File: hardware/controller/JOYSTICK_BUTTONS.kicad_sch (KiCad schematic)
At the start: 18 parts, among them SW401 UP, SW402 LEFT, SW403 DOWN, SW404 RIGHT

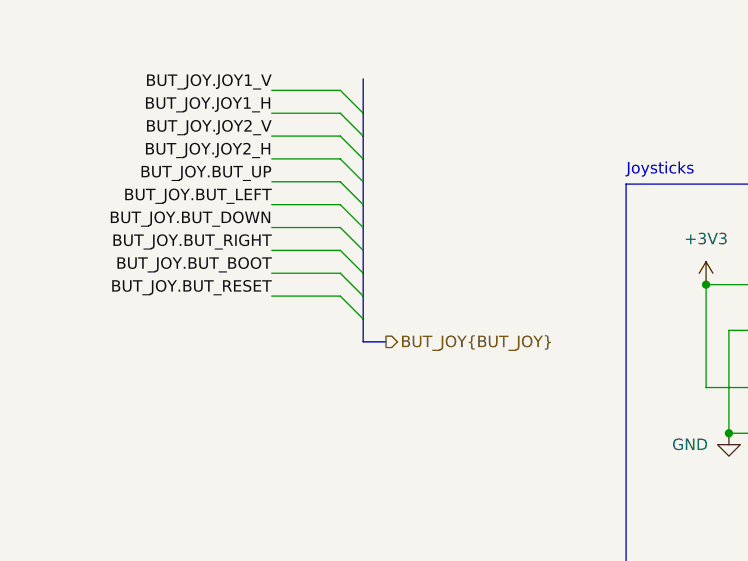
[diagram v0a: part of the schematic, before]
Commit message: fixed 3d models. rounded edges of pcb
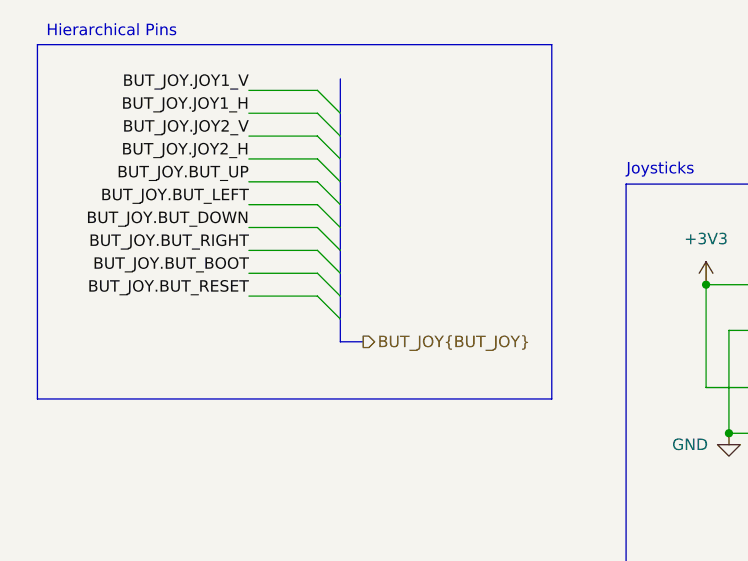
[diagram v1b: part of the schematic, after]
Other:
- note added: "Hierarchical Pins"
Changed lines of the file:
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@@
 	(paper "A4")
+	(rectangle
+		(start 14.605 15.24)
+		(end 71.755 54.61)
+		(stroke
+			(width 0)
+			(type default)
+		)
+		(fill
+			(type none)
+		)
+	)
 	(rectangle
 		(start 80.01 30.734)
@@
 		)
 	)
+	(text "Hierarchical Pins"
+		(exclude_from_sim no)
+		(at 22.86 13.843 0)
+		(effects
+			(font
+				(size 1.27 1.27)
+			)
+		)
+	)
 	(text "Joysticks"
 		(exclude_from_sim no)
@@
 	)
 	(bus_entry
-		(at 48.26 22.86)
+		(at 45.72 22.86)
 		(size 2.54 2.54)
 		(stroke
@@
 	)
 	(bus_entry
-		(at 48.26 35.56)
+		(at 45.72 35.56)
 		(size 2.54 2.54)
 		(stroke
@@
 	)
 	(bus_entry
-		(at 48.26 38.1)
+		(at 45.72 38.1)
 		(size 2.54 2.54)
 		(stroke
@@
 	)
 	(bus_entry
-		(at 48.26 40.64)
+		(at 45.72 40.64)
 		(size 2.54 2.54)
 		(stroke
@@
 	)
 	(bus_entry
-		(at 48.26 20.32)
+		(at 45.72 20.32)
 		(size 2.54 2.54)
 		(stroke
@@
 	)
 	(bus_entry
-		(at 48.26 33.02)
+		(at 45.72 33.02)
 		(size 2.54 2.54)
 		(stroke
@@
 	)
 	(bus_entry
-		(at 48.26 25.4)
+		(at 45.72 25.4)
 		(size 2.54 2.54)
 		(stroke
@@
 	)
 	(bus_entry
-		(at 48.26 27.94)
+		(at 45.72 27.94)
 		(size 2.54 2.54)
 		(stroke
@@
 	)
 	(bus_entry
-		(at 48.26 43.18)
+		(at 45.72 43.18)
 		(size 2.54 2.54)
 		(stroke
@@
 	)
 	(bus_entry
-		(at 48.26 30.48)
+		(at 45.72 30.48)
 		(size 2.54 2.54)
 		(stroke
@@
 	(bus
 		(pts
-			(xy 50.8 27.94) (xy 50.8 30.48)
+			(xy 48.26 27.94) (xy 48.26 30.48)
 		)
 		(stroke
@@
 	(bus
 		(pts
-			(xy 50.8 30.48) (xy 50.8 33.02)
+			(xy 48.26 30.48) (xy 48.26 33.02)
 		)
 		(stroke
@@
 	(bus
 		(pts
-			(xy 50.8 33.02) (xy 50.8 35.56)
+			(xy 48.26 33.02) (xy 48.26 35.56)
 		)
 		(stroke
@@
 	(bus
 		(pts
-			(xy 50.8 22.86) (xy 50.8 25.4)
+			(xy 48.26 22.86) (xy 48.26 25.4)
 		)
 		(stroke
@@
 	(bus
 		(pts
-			(xy 50.8 38.1) (xy 50.8 40.64)
-		)
-		(stroke
-			(width 0)
-			(type default)
-		)
-	)
-	(wire
-		(pts
-			(xy 40.64 27.94) (xy 48.26 27.94)
+			(xy 48.26 38.1) (xy 48.26 40.64)
+		)
+		(stroke
+			(width 0)
+			(type default)
+		)
+	)
+	(wire
+		(pts
+			(xy 38.1 27.94) (xy 45.72 27.94)
 		)
 		(stroke
@@
 	(bus
 		(pts
-			(xy 50.8 35.56) (xy 50.8 38.1)
+			(xy 48.26 35.56) (xy 48.26 38.1)
 		)
 		(stroke
@@
 	(wire
 		(pts
-			(xy 40.64 33.02) (xy 48.26 33.02)
+			(xy 38.1 33.02) (xy 45.72 33.02)
 		)
 		(stroke
@@
 	(bus
 		(pts
-			(xy 50.8 43.18) (xy 50.8 45.72)
+			(xy 48.26 43.18) (xy 48.26 45.72)
 		)
 		(stroke
@@
 	(bus
 		(pts
-			(xy 50.8 45.72) (xy 50.8 48.26)
+			(xy 48.26 45.72) (xy 48.26 48.26)
 		)
 		(stroke
@@
 	(wire
 		(pts
-			(xy 40.64 40.64) (xy 48.26 40.64)
+			(xy 38.1 40.64) (xy 45.72 40.64)
 		)
 		(stroke
@@
 	(wire
 		(pts
-			(xy 40.64 38.1) (xy 48.26 38.1)
+			(xy 38.1 38.1) (xy 45.72 38.1)
 		)
 		(stroke
@@
 	(bus
 		(pts
-			(xy 50.8 19.05) (xy 50.8 22.86)
+			(xy 48.26 19.05) (xy 48.26 22.86)
 		)
 		(stroke
@@
 	(wire
 		(pts
-			(xy 40.64 35.56) (xy 48.26 35.56)
+			(xy 38.1 35.56) (xy 45.72 35.56)
 		)
 		(stroke
@@
 	(bus
 		(pts
-			(xy 50.8 48.26) (xy 53.34 48.26)
+			(xy 48.26 48.26) (xy 50.8 48.26)
 		)
 		(stroke
@@
 	(bus
 		(pts
-			(xy 50.8 40.64) (xy 50.8 43.18)
+			(xy 48.26 40.64) (xy 48.26 43.18)
 		)
 		(stroke
@@
 	(wire
 		(pts
-			(xy 40.64 30.48) (xy 48.26 30.48)
+			(xy 38.1 30.48) (xy 45.72 30.48)
 		)
 		(stroke
@@
 	(wire
 		(pts
-			(xy 40.64 43.18) (xy 48.26 43.18)
+			(xy 38.1 43.18) (xy 45.72 43.18)
 		)
 		(stroke
@@
 	(wire
 		(pts
-			(xy 40.64 20.32) (xy 48.26 20.32)
+			(xy 38.1 20.32) (xy 45.72 20.32)
 		)
 		(stroke
@@
 	(bus
 		(pts
-			(xy 50.8 25.4) (xy 50.8 27.94)
+			(xy 48.26 25.4) (xy 48.26 27.94)
 		)
 		(stroke
@@
 	(wire
 		(pts
-			(xy 40.64 22.86) (xy 48.26 22.86)
+			(xy 38.1 22.86) (xy 45.72 22.86)
 		)
 		(stroke
@@
 	(wire
 		(pts
-			(xy 40.64 25.4) (xy 48.26 25.4)
+			(xy 38.1 25.4) (xy 45.72 25.4)
 		)
 		(stroke
@@
 	)
 	(label "BUT_JOY.JOY1_V"
-		(at 40.64 20.32 180)
+		(at 38.1 20.32 180)
 		(effects
 			(font
@@
 	)
 	(label "BUT_JOY.BUT_DOWN"
-		(at 40.64 35.56 180)
+		(at 38.1 35.56 180)
 		(effects
 			(font
@@
 	)
 	(label "BUT_JOY.BUT_LEFT"
-		(at 40.64 33.02 180)
+		(at 38.1 33.02 180)
 		(effects
 			(font
@@
 	)
 	(label "BUT_JOY.BUT_RESET"
-		(at 40.64 43.18 180)
+		(at 38.1 43.18 180)
 		(effects
 			(font
@@
 	)
 	(label "BUT_JOY.BUT_UP"
-		(at 40.64 30.48 180)
+		(at 38.1 30.48 180)
 		(effects
 			(font
@@
 	)
 	(label "BUT_JOY.BUT_RIGHT"
-		(at 40.64 38.1 180)
+		(at 38.1 38.1 180)
 		(effects
 			(font
@@
 	)
 	(label "BUT_JOY.JOY2_H"
-		(at 40.64 27.94 180)
+		(at 38.1 27.94 180)
 		(effects
 			(font
@@
 	)
 	(label "BUT_JOY.JOY2_V"
-		(at 40.64 25.4 180)
+		(at 38.1 25.4 180)
 		(effects
 			(font
@@
 	)
 	(label "BUT_JOY.BUT_BOOT"
-		(at 40.64 40.64 180)
+		(at 38.1 40.64 180)
 		(effects
 			(font
@@
 	)
 	(label "BUT_JOY.JOY1_H"
-		(at 40.64 22.86 180)
+		(at 38.1 22.86 180)
 		(effects
 			(font
@@
 	(hierarchical_label "BUT_JOY{BUT_JOY}"
 		(shape output)
-		(at 53.34 48.26 0)
-		(effects
-			(font
+		(at 50.8 48.26 0)
+		(effects
+			(font

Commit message: a
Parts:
- R401, R402, R403, R404, R405, R406: footprint SamacSys_Parts:RESC2012X60N -> RESC2012X60N
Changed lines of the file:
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@@
 			)
 		)
-		(property "Footprint" "SamacSys_Parts:RESC2012X60N"
+		(property "Footprint" "RESC2012X60N"
 			(at 121.92 262.56 0)
 			(effects
@@
 			)
 		)
-		(property "Datasheet" "~"
+		(property "Datasheet" "https://componentsearchengine.com/Datasheets/2/ASC0805-10KFT5.pdf"
 			(at 121.92 362.56 0)
 			(effects
@@
 			)
 		)
-		(property "Description" "Resistor"
+		(property "Description" "WELWYN - ASC0805-10KFT5 - RESISTOR, ANTI SULPHUR, 10K, 0.125W, 1%"
 			(at 107.95 166.37 0)
 			(effects
@@
 			)
 		)
-		(property "Footprint" "SamacSys_Parts:RESC2012X60N"
+		(property "Footprint" "RESC2012X60N"
 			(at 162.56 262.56 0)
 			(effects
@@
 			)
 		)
-		(property "Datasheet" "~"
+		(property "Datasheet" "https://componentsearchengine.com/Datasheets/2/ASC0805-10KFT5.pdf"
 			(at 162.56 362.56 0)
 			(effects
@@
 			)
 		)
-		(property "Description" "Resistor"
+		(property "Description" "WELWYN - ASC0805-10KFT5 - RESISTOR, ANTI SULPHUR, 10K, 0.125W, 1%"
 			(at 148.59 166.37 0)
 			(effects
@@
 			)
 		)
-		(property "Footprint" "SamacSys_Parts:RESC2012X60N"
+		(property "Footprint" "RESC2012X60N"
 			(at 182.88 166.04 0)
 			(effects
@@
 			)
 		)
-		(property "Datasheet" "~"
+		(property "Datasheet" "https://componentsearchengine.com/Datasheets/2/ASC0805-10KFT5.pdf"
 			(at 182.88 266.04 0)
 			(effects
@@
 			)
 		)
-		(property "Description" "Resistor"
+		(property "Description" "WELWYN - ASC0805-10KFT5 - RESISTOR, ANTI SULPHUR, 10K, 0.125W, 1%"
 			(at 168.91 69.85 0)
 			(effects
@@
 			)
 		)
-		(property "Footprint" "SamacSys_Parts:RESC2012X60N"
+		(property "Footprint" "RESC2012X60N"
 			(at 100.33 261.29 0)
 			(effects
@@
 			)
 		)
-		(property "Datasheet" "~"
+		(property "Datasheet" "https://componentsearchengine.com/Datasheets/2/ASC0805-10KFT5.pdf"
 			(at 100.33 361.29 0)
 			(effects
@@
 			)
 		)
-		(property "Description" "Resistor"
+		(property "Description" "WELWYN - ASC0805-10KFT5 - RESISTOR, ANTI SULPHUR, 10K, 0.125W, 1%"
 			(at 86.36 165.1 0)
 			(effects
@@
 			)
 		)
-		(property "Footprint" "SamacSys_Parts:RESC2012X60N"
+		(property "Footprint" "RESC2012X60N"
 			(at 142.24 262.56 0)
 			(effects
@@
 			)
 		)
-		(property "Datasheet" "~"
+		(property "Datasheet" "https://componentsearchengine.com/Datasheets/2/ASC0805-10KFT5.pdf"
 			(at 142.24 362.56 0)
 			(effects
@@
 			)
 		)
-		(property "Description" "Resistor"
+		(property "Description" "WELWYN - ASC0805-10KFT5 - RESISTOR, ANTI SULPHUR, 10K, 0.125W, 1%"
 			(at 128.27 166.37 0)
 			(effects
@@
 			)
 		)
-		(property "Footprint" "SamacSys_Parts:RESC2012X60N"
+		(property "Footprint" "RESC2012X60N"
 			(at 207.01 166.04 0)
 			(effects
@@
 			)
 		)
-		(property "Datasheet" "~"
+		(property "Datasheet" "https://componentsearchengine.com/Datasheets/2/ASC0805-10KFT5.pdf"
 			(at 207.01 266.04 0)
 			(effects
@@
 			)
 		)
-		(property "Description" "Resistor"
+		(property "Description" "WELWYN - ASC0805-10KFT5 - RESISTOR, ANTI SULPHUR, 10K, 0.125W, 1%"
 			(at 193.04 69.85 0)
 			(effects

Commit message: save before nuke
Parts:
- R108: renamed from R401; footprint RESC2012X60N -> SamacSys_Parts:RESC2012X60N
- R109: renamed from R402; footprint RESC2012X60N -> SamacSys_Parts:RESC2012X60N
- R110: renamed from R403; footprint RESC2012X60N -> SamacSys_Parts:RESC2012X60N
- R111: renamed from R404; footprint RESC2012X60N -> SamacSys_Parts:RESC2012X60N
- R112: renamed from R405; footprint RESC2012X60N -> SamacSys_Parts:RESC2012X60N
- R113: renamed from R406; footprint RESC2012X60N -> SamacSys_Parts:RESC2012X60N
- renumbered S401 to S101, S402 to S102, SW401 to SW101, SW402 to SW102, SW403 to SW103, SW404 to SW104, TP401 to TP106, TP402 to TP107, TP403 to TP108, TP404 to TP109, VR401 to VR101, VR402 to VR102

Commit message: done but need to add stitching vias
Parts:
- TP106, TP107, TP108, TP109: footprint TestPoint:TestPoint_Pad_1.0x1.0mm -> SamacSys_Parts:TestPoint_Pad_1.0x1.0mm
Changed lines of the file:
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@@
 			)
 		)
-		(property "Footprint" "TestPoint:TestPoint_Pad_1.0x1.0mm"
+		(property "Footprint" "SamacSys_Parts:TestPoint_Pad_1.0x1.0mm"
 			(at 134.62 55.88 0)
 			(effects
@@
 			)
 		)
-		(property "Footprint" "TestPoint:TestPoint_Pad_1.0x1.0mm"
+		(property "Footprint" "SamacSys_Parts:TestPoint_Pad_1.0x1.0mm"
 			(at 134.62 93.98 0)
 			(effects
@@
 			)
 		)
-		(property "Footprint" "TestPoint:TestPoint_Pad_1.0x1.0mm"
+		(property "Footprint" "SamacSys_Parts:TestPoint_Pad_1.0x1.0mm"
 			(at 134.62 105.41 0)
 			(effects
@@
 			)
 		)
-		(property "Footprint" "TestPoint:TestPoint_Pad_1.0x1.0mm"
+		(property "Footprint" "SamacSys_Parts:TestPoint_Pad_1.0x1.0mm"
 			(at 134.62 44.45 0)
 			(effects

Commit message: forgor
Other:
- note added: "SMD BOOT & RESET Buttons"
- note removed: "SMT BOOT & RESET Buttons"
- moved on the sheet: R108, R109, R110, R111, R112, R113, S101, S102, SW101, SW102, SW103, SW104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

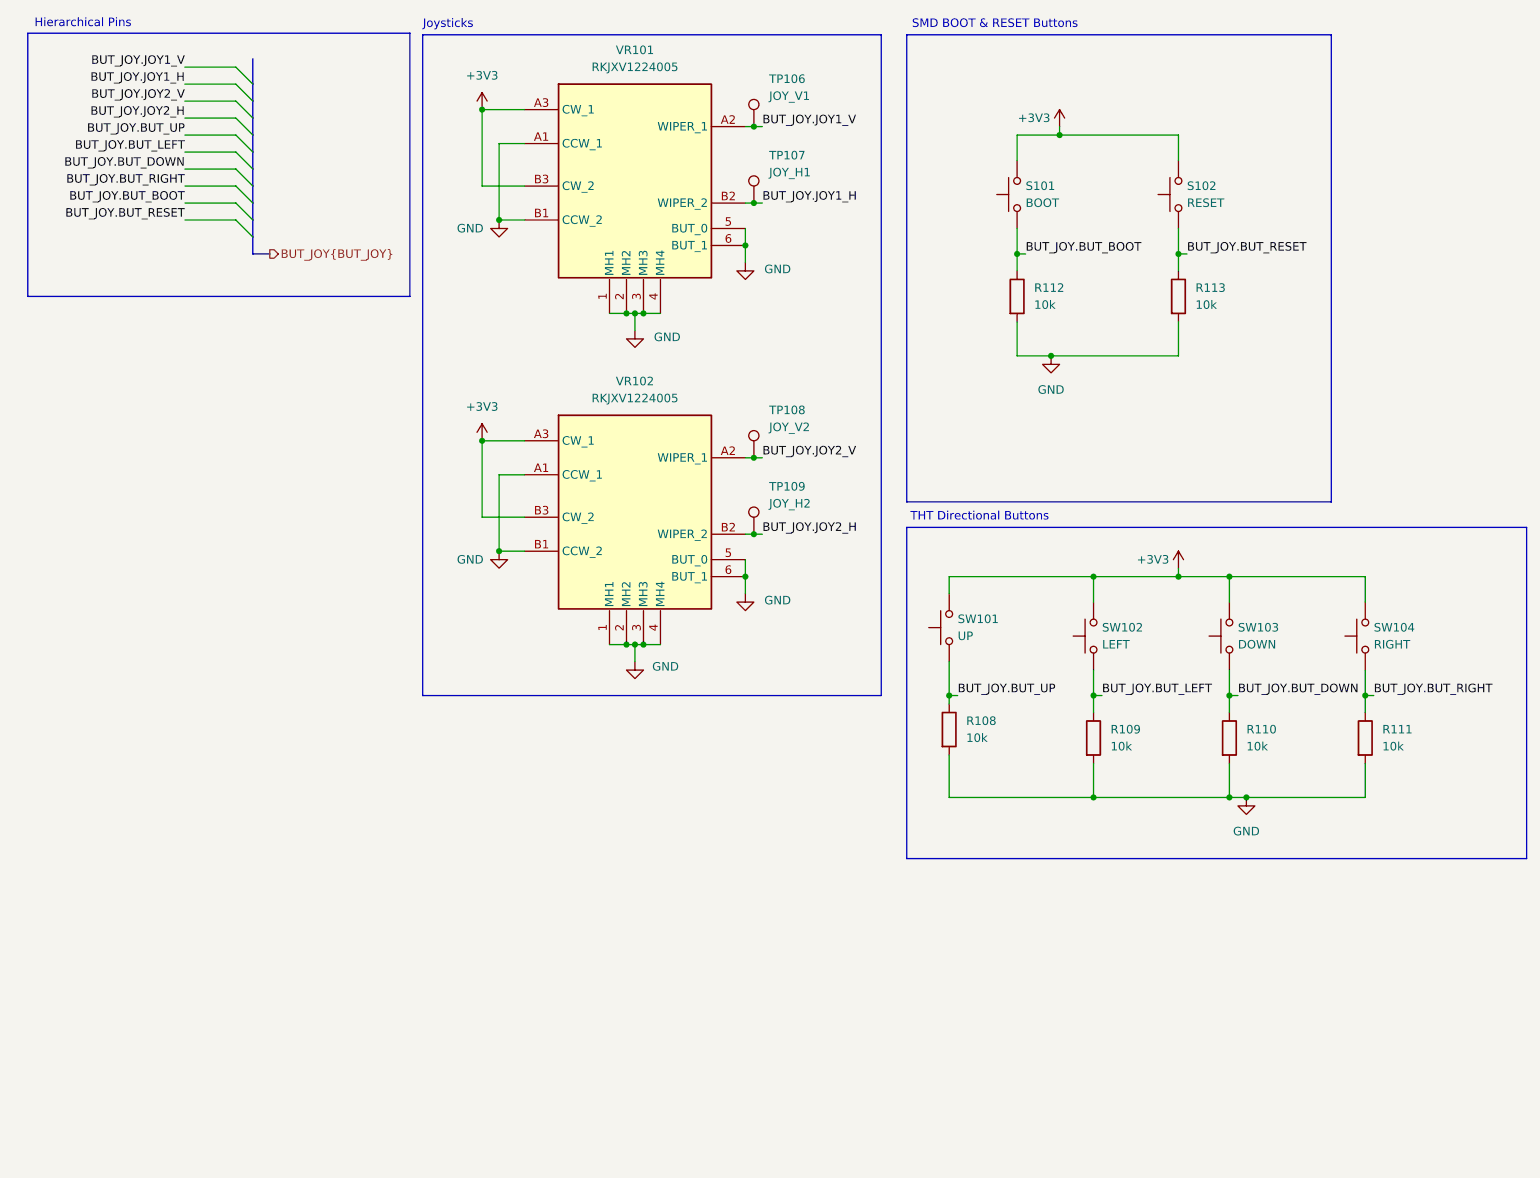
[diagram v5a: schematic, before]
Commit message: clean up DRC. need to add stitching vias and figure out why inner ground plane isnt connected to F.Cu pour
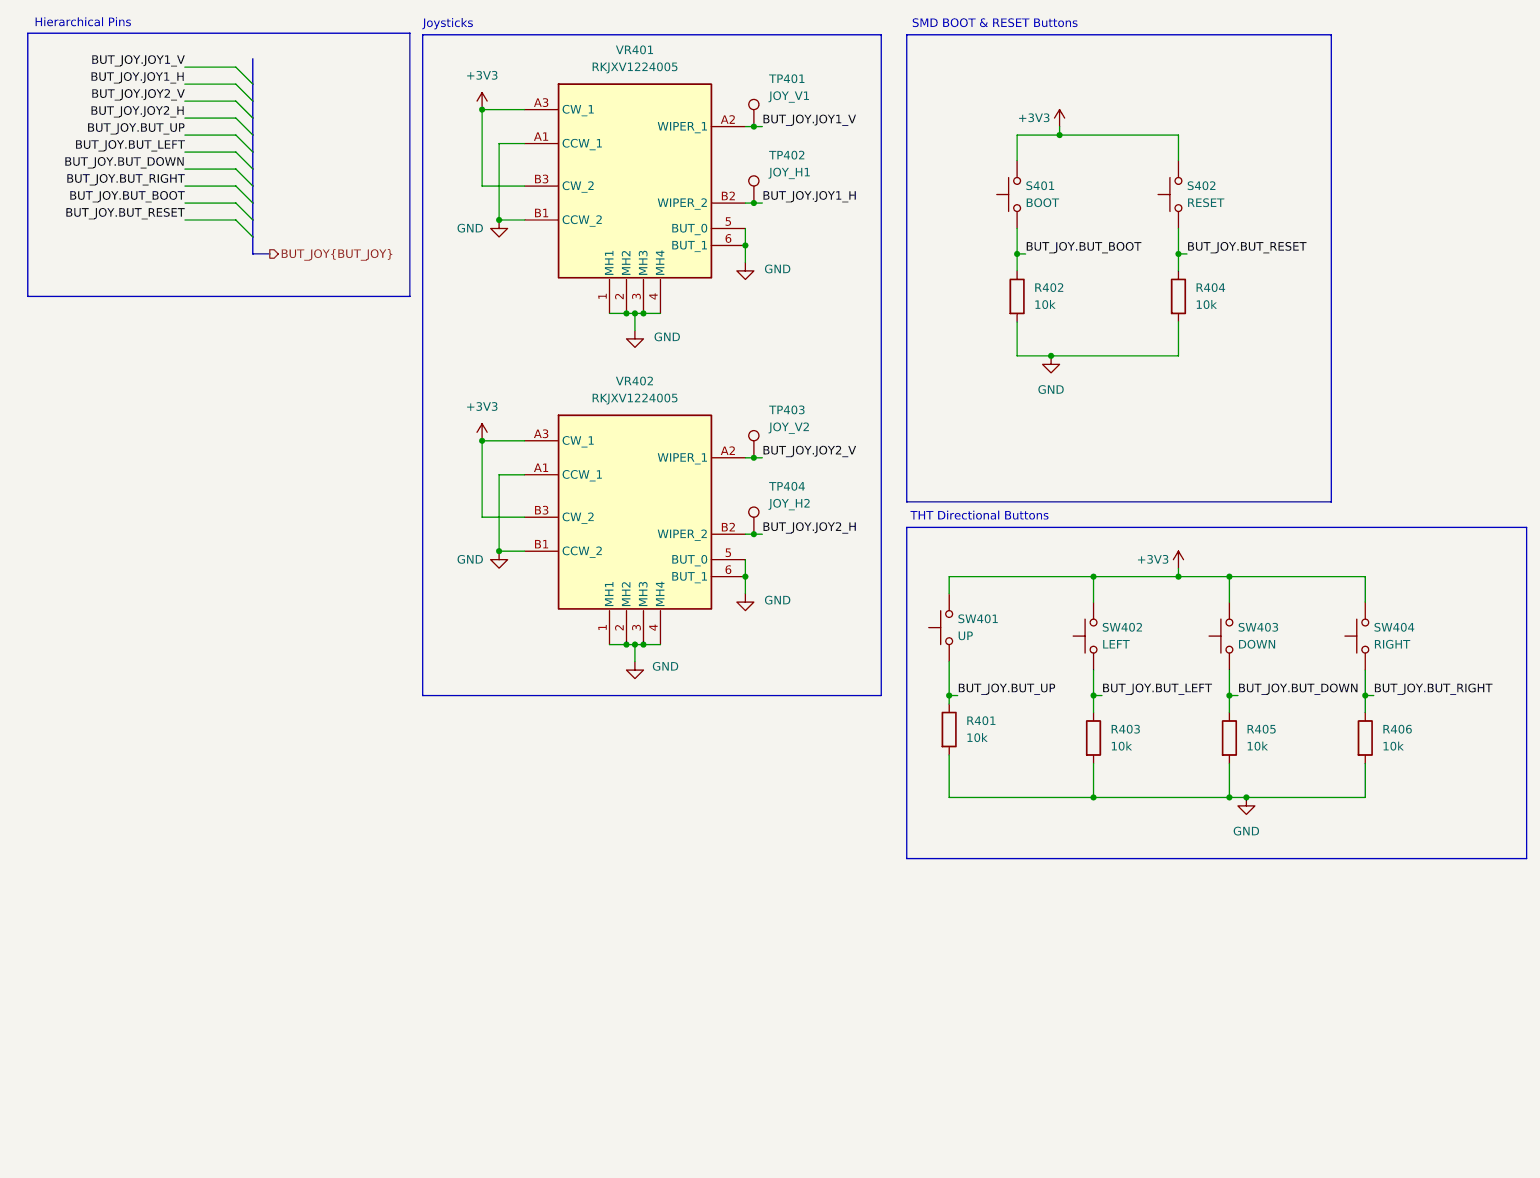
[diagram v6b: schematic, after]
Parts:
- renumbered R108 to R401, R112 to R402, R109 to R403, R113 to R404, R110 to R405, R111 to R406, S101 to S401, S102 to S402, SW101 to SW401, SW102 to SW402, SW103 to SW403, SW104 to SW404, TP106 to TP401, TP107 to TP402, TP108 to TP403, TP109 to TP404, VR101 to VR401, VR102 to VR402
